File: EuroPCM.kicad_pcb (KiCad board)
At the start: 2 copper layers, 160 x 100 mm, 5 parts, among them IC1 TDA1541A

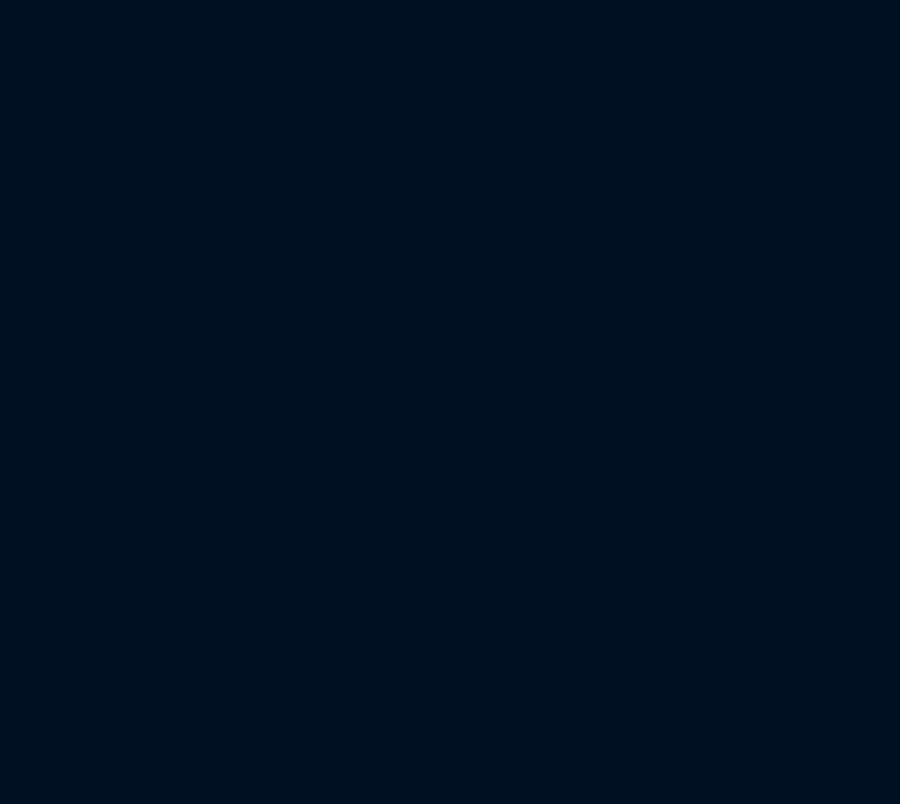
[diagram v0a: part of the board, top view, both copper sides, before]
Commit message: Add tda1315 footprint use schematic sheets
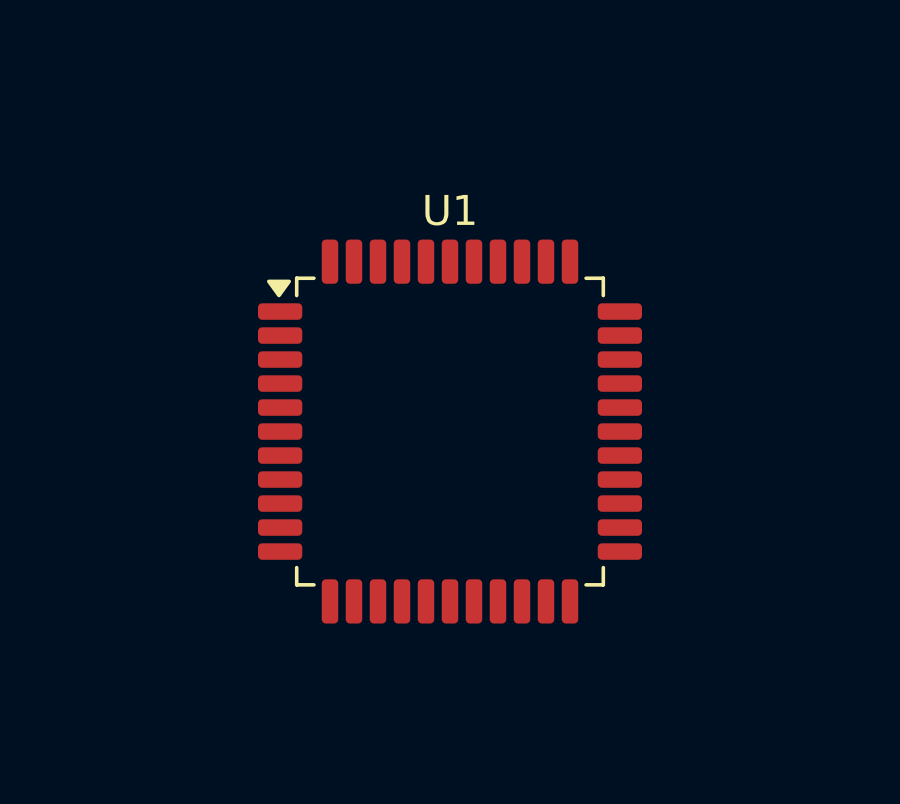
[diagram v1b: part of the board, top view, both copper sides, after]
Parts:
- added U1: ~, Package_QFP:LQFP-44_10x10mm_P0.8mm, F.Cu at (92.4, 90.3)

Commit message: Add decoupling transformer
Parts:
- added T1: PE-65612NL, Library:PE65612NL, F.Cu at (67.8, 93.1)

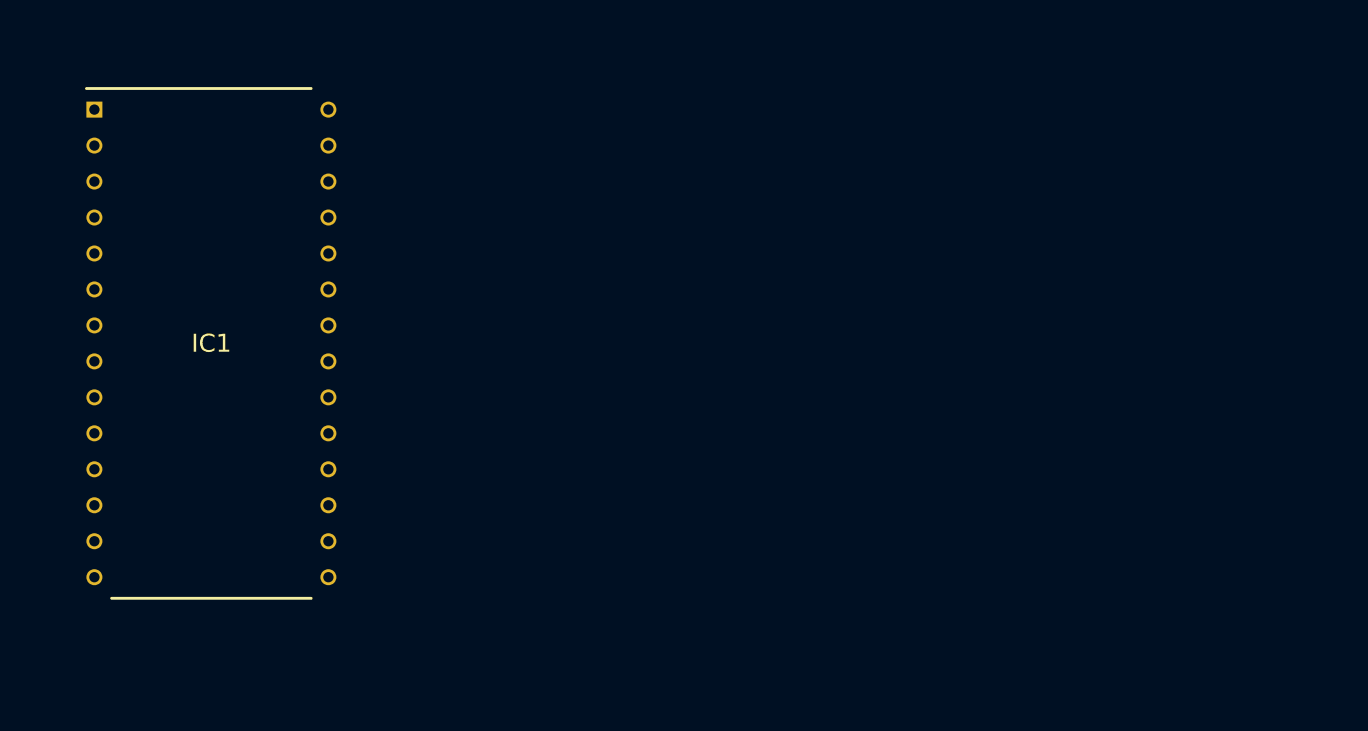
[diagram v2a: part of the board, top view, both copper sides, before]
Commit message: Add DAC caps
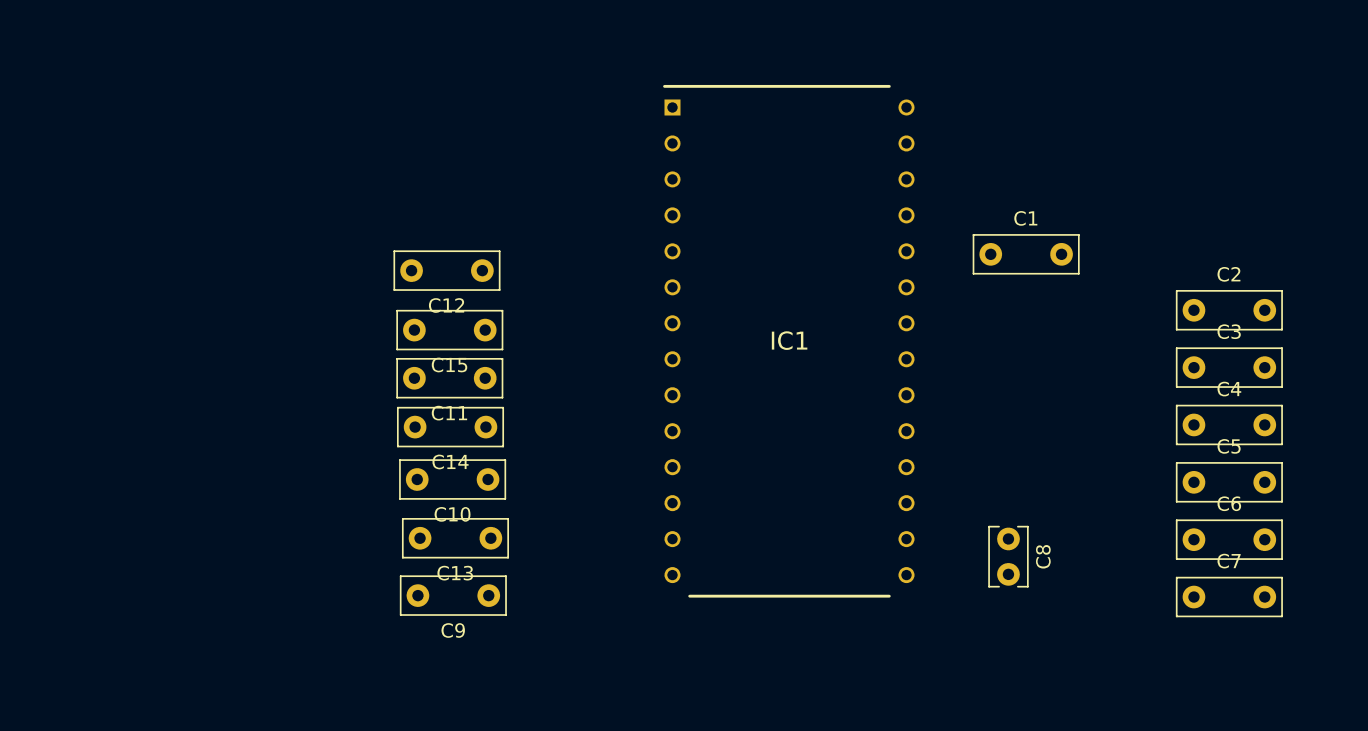
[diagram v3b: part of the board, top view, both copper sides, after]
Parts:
- added C1: 0.1, Capacitor_THT:C_Rect_L7.2mm_W2.5mm_P5.00mm_FKS2_FKP2_MKS2_MKP2, F.Cu at (187.5, 83.5)
- added C10: 0.1, Capacitor_THT:C_Rect_L7.2mm_W2.5mm_P5.00mm_FKS2_FKP2_MKS2_MKP2, F.Cu at (152.0, 99.4)
- added C11: 0.1, Capacitor_THT:C_Rect_L7.2mm_W2.5mm_P5.00mm_FKS2_FKP2_MKS2_MKP2, F.Cu at (151.8, 92.2)
- added C12: 0.1, Capacitor_THT:C_Rect_L7.2mm_W2.5mm_P5.00mm_FKS2_FKP2_MKS2_MKP2, F.Cu at (151.6, 84.7)
- added C13: 0.1, Capacitor_THT:C_Rect_L7.2mm_W2.5mm_P5.00mm_FKS2_FKP2_MKS2_MKP2, F.Cu at (152.2, 103.5)
- added C14: 0.1, Capacitor_THT:C_Rect_L7.2mm_W2.5mm_P5.00mm_FKS2_FKP2_MKS2_MKP2, F.Cu at (151.8, 95.7)
- added C15: 0.1, Capacitor_THT:C_Rect_L7.2mm_W2.5mm_P5.00mm_FKS2_FKP2_MKS2_MKP2, F.Cu at (151.8, 88.8)
- added C2: 0.1, Capacitor_THT:C_Rect_L7.2mm_W2.5mm_P5.00mm_FKS2_FKP2_MKS2_MKP2, F.Cu at (201.8, 87.5)
- added C3: 0.1, Capacitor_THT:C_Rect_L7.2mm_W2.5mm_P5.00mm_FKS2_FKP2_MKS2_MKP2, F.Cu at (201.8, 91.5)
- added C4: 0.1, Capacitor_THT:C_Rect_L7.2mm_W2.5mm_P5.00mm_FKS2_FKP2_MKS2_MKP2, F.Cu at (201.8, 95.5)
- added C5: 0.1, Capacitor_THT:C_Rect_L7.2mm_W2.5mm_P5.00mm_FKS2_FKP2_MKS2_MKP2, F.Cu at (201.8, 99.6)
- added C6: 0.1, Capacitor_THT:C_Rect_L7.2mm_W2.5mm_P5.00mm_FKS2_FKP2_MKS2_MKP2, F.Cu at (201.8, 103.7)
- added C7: 0.1, Capacitor_THT:C_Rect_L7.2mm_W2.5mm_P5.00mm_FKS2_FKP2_MKS2_MKP2, F.Cu at (201.8, 107.7)
- added C8: 680p, Capacitor_THT:C_Rect_L4.0mm_W2.5mm_P2.50mm, F.Cu at (188.7, 103.6)
- added C9: 0.1, Capacitor_THT:C_Rect_L7.2mm_W2.5mm_P5.00mm_FKS2_FKP2_MKS2_MKP2, F.Cu at (152.0, 107.6)
- moved IC1 40.8 mm to (173.3, 89.6)
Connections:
- IC1 pad 10: unconnected-(IC1-DECOU_4-Pad10) -> Net-(IC1-DECOU_4)
- IC1 pad 11: unconnected-(IC1-DECOU_5-Pad11) -> Net-(IC1-DECOU_5)
- IC1 pad 12: unconnected-(IC1-DECOU_6-Pad12) -> Net-(IC1-DECOU_6)
- IC1 pad 14: unconnected-(IC1-GND_(D)-Pad14) -> GND
- IC1 pad 16: unconnected-(IC1-COSC_1-Pad16) -> Net-(IC1-COSC_1)
- IC1 pad 17: unconnected-(IC1-COSC_2-Pad17) -> Net-(IC1-COSC_2)
- IC1 pad 18: unconnected-(IC1-DECOU_8-Pad18) -> Net-(IC1-DECOU_8)
- IC1 pad 19: unconnected-(IC1-DECOU_9-Pad19) -> Net-(IC1-DECOU_9)
- IC1 pad 20: unconnected-(IC1-DECOU_10-Pad20) -> Net-(IC1-DECOU_10)
- IC1 pad 21: unconnected-(IC1-DECOU_11-Pad21) -> Net-(IC1-DECOU_11)
- IC1 pad 22: unconnected-(IC1-DECOU_12-Pad22) -> Net-(IC1-DECOU_12)
- IC1 pad 23: unconnected-(IC1-DECOU_13-Pad23) -> Net-(IC1-DECOU_13)
- IC1 pad 24: unconnected-(IC1-DECOU_14-Pad24) -> Net-(IC1-DECOU_14)
- IC1 pad 5: unconnected-(IC1-GND_(A)-Pad5) -> GND
- IC1 pad 6: unconnected-(IC1-AOR-Pad6) -> Net-(IC1-AOR)
- IC1 pad 7: unconnected-(IC1-DECOU_1-Pad7) -> Net-(IC1-DECOU_1)
- IC1 pad 8: unconnected-(IC1-DECOU_2-Pad8) -> Net-(IC1-DECOU_2)
- IC1 pad 9: unconnected-(IC1-DECOU_3-Pad9) -> Net-(IC1-DECOU_3)

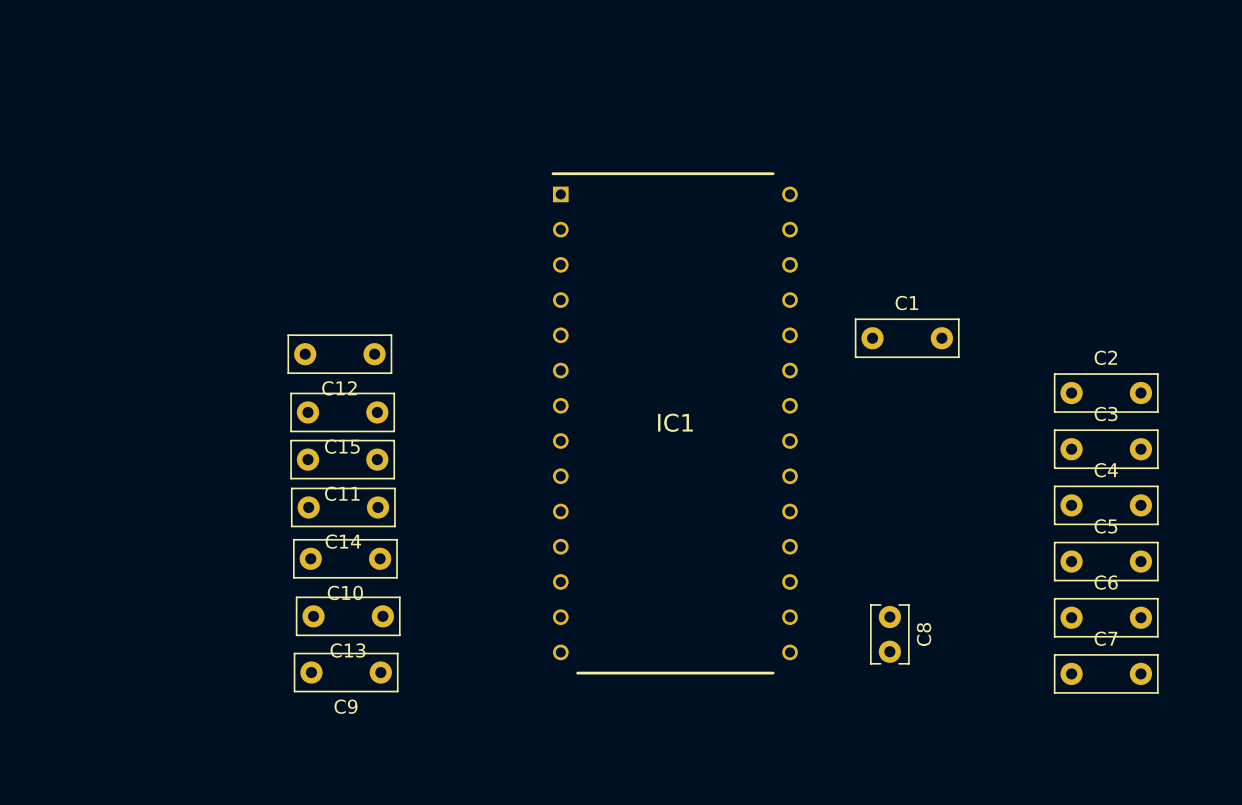
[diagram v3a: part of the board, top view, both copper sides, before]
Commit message: Add amplifier circuit
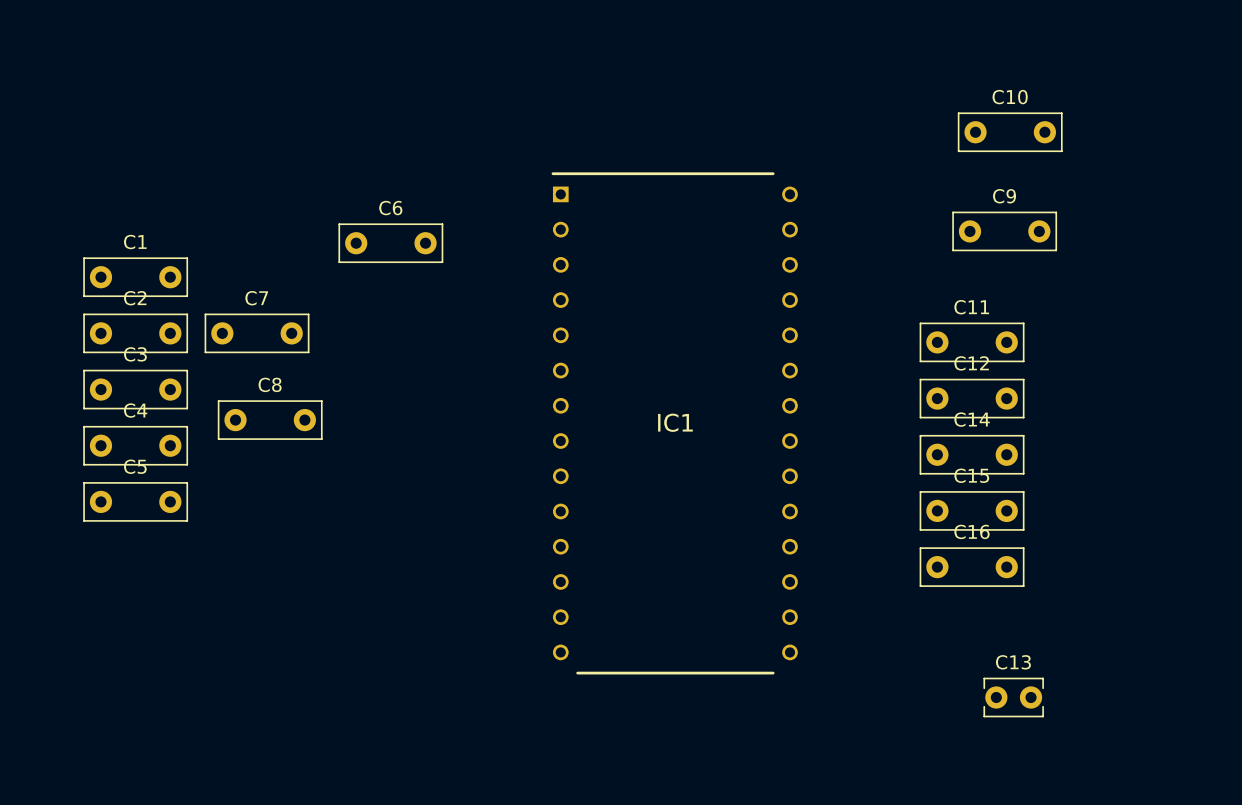
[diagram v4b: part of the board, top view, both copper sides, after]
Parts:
- added C16: 0.1, Capacitor_THT:C_Rect_L7.2mm_W2.5mm_P5.00mm_FKS2_FKP2_MKS2_MKP2, F.Cu at (192.2, 100.0)
- C13: value 0.1 -> 680p; footprint Capacitor_THT:C_Rect_L7.2mm_W2.5mm_P5.00mm_FKS2_FKP2_MKS2_MKP2 -> Capacitor_THT:C_Rect_L4.0mm_W2.5mm_P2.50mm
- C8: value 680p -> 0.1; footprint Capacitor_THT:C_Rect_L4.0mm_W2.5mm_P2.50mm -> Capacitor_THT:C_Rect_L7.2mm_W2.5mm_P5.00mm_FKS2_FKP2_MKS2_MKP2
- moved C2 70.1 mm to (131.8, 83.2)
- moved C3 70.1 mm to (131.8, 87.2)
- moved C4 70.1 mm to (131.8, 91.2)
- moved C5 70.1 mm to (131.8, 95.3)
- moved C7 66.0 mm to (140.6, 83.2)
- moved C6 58.2 mm to (150.2, 76.7)
- moved C1 55.8 mm to (131.8, 79.1)
- moved C9 53.1 mm to (194.5, 75.8), turned to 0 degrees
- moved C10 52.8 mm to (194.9, 68.7), turned to 0 degrees
- moved C8 49.3 mm to (141.6, 89.4), turned to 0 degrees
- moved C13 44.6 mm to (196.4, 109.4), turned to 0 degrees
- moved C11 41.3 mm to (192.2, 83.8), turned to 0 degrees
- moved C15 41.0 mm to (192.2, 96.0), turned to 0 degrees
- moved C12 40.7 mm to (192.2, 87.8), turned to 0 degrees
- moved C14 40.5 mm to (192.2, 91.9), turned to 0 degrees
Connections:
- C1 pad 1: Net-(IC1-DECOU_14) -> Net-(IC1-DECOU_1)
- C10 pad 1: Net-(IC1-DECOU_4) -> Net-(IC1-DECOU_12)
- C11 pad 1: Net-(IC1-DECOU_2) -> Net-(IC1-DECOU_10)
- C12 pad 1: Net-(IC1-AOR) -> Net-(IC1-DECOU_8)
- C13 pad 1: Net-(IC1-DECOU_5) -> Net-(IC1-COSC_2)
- C13 pad 2: GND -> Net-(IC1-COSC_1)
- C14 pad 1: Net-(IC1-DECOU_3) -> Net-(IC1-DECOU_13)
- C15 pad 1: Net-(IC1-DECOU_1) -> Net-(IC1-DECOU_11)
- C2 pad 1: Net-(IC1-DECOU_13) -> Net-(IC1-DECOU_3)
- C3 pad 1: Net-(IC1-DECOU_12) -> Net-(IC1-DECOU_5)
- C4 pad 1: Net-(IC1-DECOU_11) -> Net-(IC1-DECOU_7)
- C5 pad 1: Net-(IC1-DECOU_10) -> Net-(IC1-AOR)
- C6 pad 1: Net-(IC1-DECOU_9) -> Net-(IC1-DECOU_2)
- C7 pad 1: Net-(IC1-DECOU_8) -> Net-(IC1-DECOU_4)
- C8 pad 1: Net-(IC1-COSC_2) -> Net-(IC1-DECOU_6)
- C8 pad 2: Net-(IC1-COSC_1) -> GND
- C9 pad 1: Net-(IC1-DECOU_6) -> Net-(IC1-DECOU_14)
- IC1 pad 13: unconnected-(IC1-DECOU_7-Pad13) -> Net-(IC1-DECOU_7)
